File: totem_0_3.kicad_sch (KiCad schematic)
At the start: 88 parts, among them J1 MJ-4PP-9, J2 MJ-4PP-9, U1 xiao-ble, U2 xiao-ble

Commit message: Switch from matrix switches to direct connect
Added two rp2040's to schema
Leaving out lables on rp2040 to make routing easier later
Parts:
- removed DL1, DL10, DL11, DL12, DL13, DL14, DL15, DL16, DL17, DL18, DL19, DL2, DL3, DL4, DL5, DL6, DL7, DL8, DL9, DR1, DR10, DR11, DR12, DR13, DR14, DR15, DR16, DR17, DR18, DR19, DR2, DR3, DR4, DR5, DR6, DR7, DR8, DR9: D_Small, TOTEMlib:Diode_SOD123, symbol Device:D_Small
- added U3, U4: RP2040, Package_DFN_QFN:QFN-56-1EP_7x7mm_P0.4mm_EP3.2x3.2mm, symbol MCU_RaspberryPi:RP2040
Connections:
- net COL0_L: no longer SWL1.1, SWL11.1, SWL16.1, SWL6.1
- net COL0_R: no longer SWR1.1, SWR11.1, SWR16.1, SWR6.1
- net COL1_L: no longer SWL12.1, SWL2.1, SWL7.1
- net COL1_R: no longer SWR12.1, SWR2.1, SWR7.1
- net COL2_L: no longer SWL13.1, SWL17.1, SWL3.1, SWL8.1
- net COL2_R: no longer SWR13.1, SWR17.1, SWR3.1, SWR8.1
- net COL3_L: no longer SWL14.1, SWL18.1, SWL4.1, SWL9.1
- net COL3_R: no longer SWR14.1, SWR18.1, SWR4.1, SWR9.1
- net COL4_L: no longer SWL10.1, SWL15.1, SWL19.1, SWL5.1
- net COL4_R: no longer SWR10.1, SWR15.1, SWR19.1, SWR5.1
- net GND_L: now also SWL1.2, SWL10.2, SWL11.2, SWL13.2, SWL14.2, SWL15.2, SWL16.2, SWL17.2, SWL18.2, SWL19.2, SWL3.2, SWL4.2, SWL5.2, SWL6.2, SWL7.2, SWL8.2, SWL9.2
- net GND_R: now also SWR1.2, SWR10.2, SWR11.2, SWR12.2, SWR13.2, SWR14.2, SWR15.2, SWR16.2, SWR17.2, SWR18.2, SWR19.2, SWR2.2, SWR3.2, SWR4.2, SWR5.2, SWR6.2, SWR7.2, SWR8.2, SWR9.2
- new net: U3.1 (IOVDD), U3.10 (IOVDD), U3.22 (IOVDD), U3.33 (IOVDD), U3.42 (IOVDD), U3.49 (IOVDD)
- new net: U3.23 (DVDD), U3.50 (DVDD)
- new net: U4.1 (IOVDD), U4.10 (IOVDD), U4.22 (IOVDD), U4.33 (IOVDD), U4.42 (IOVDD), U4.49 (IOVDD)
- new net: U4.23 (DVDD), U4.50 (DVDD)
- new net SWL1: SWL1.1
- new net SWL10: SWL10.1
- new net SWL11: SWL11.1
- new net SWL12: SWL12.1
- new net SWL13: SWL13.1
- new net SWL14: SWL14.1
- new net SWL15: SWL15.1
- new net SWL16: SWL16.1, SWL6.1
- new net SWL17: SWL17.1
- new net SWL18: SWL18.1
- new net SWL19: SWL19.1
- new net SWL3: SWL3.1
- new net SWL4: SWL4.1
- new net SWL5: SWL5.1
- new net SWL7: SWL7.1
- new net SWL8: SWL8.1
- new net SWL9: SWL9.1
- new net SWR1: SWR1.1
- new net SWR10: SWR10.1
- new net SWR11: SWR11.1
- new net SWR12: SWR12.1
- new net SWR13: SWR13.1
- new net SWR14: SWR14.1
- new net SWR15: SWR15.1
- new net SWR16: SWR16.1
- new net SWR17: SWR17.1
- new net SWR18: SWR18.1
- new net SWR19: SWR19.1
- new net SWR2: SWR2.1
- new net SWR3: SWR3.1
- new net SWR4: SWR4.1
- new net SWR5: SWR5.1
- new net SWR6: SWR6.1
- new net SWR7: SWR7.1
- new net SWR8: SWR8.1
- new net SWR9: SWR9.1
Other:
- note added: "S W I T C H E S"
- note removed: "S W I T C H M A T R I X"
- moved on the sheet: BAT+1, BATGND1, PSW1, SWL1, SWL10, SWL11, SWL12, SWL13, SWL14, SWL15, SWL16, SWL17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

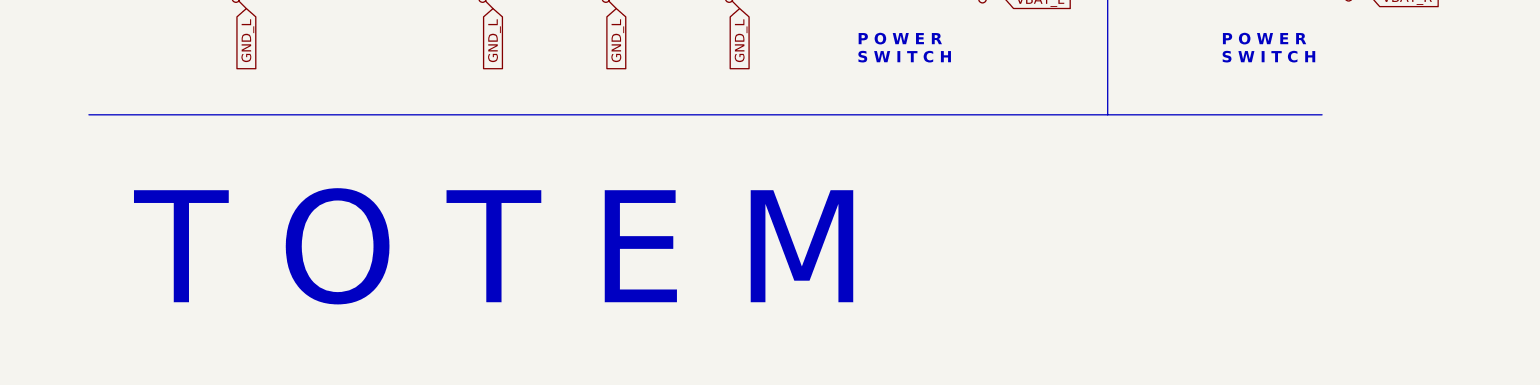
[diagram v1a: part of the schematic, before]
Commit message: Change schematic info
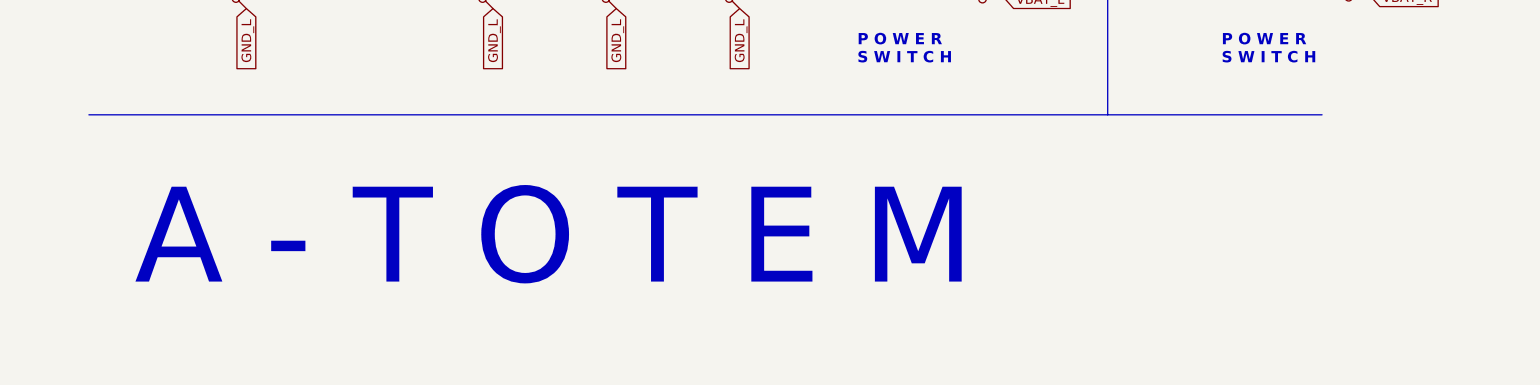
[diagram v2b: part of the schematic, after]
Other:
- note added: "A - T O T E M"
- note removed: "T O T E M"
- title: TOTEM split keyboard -> RP2040 TOTEM split keyboard
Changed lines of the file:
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@@
 	(paper "A4")
 	(title_block
-		(title "TOTEM split keyboard")
+		(title "RP2040 TOTEM split keyboard")
 		(date "2022-11-09")
 		(rev "0.3")
-		(comment 1 "made by GEIST")
+		(comment 1 "https://github.com/GEIGEIGEIST/TOTEM")
+		(comment 2 "original made by GEIST")
+		(comment 3 "made by A-Helberg")
 	)
 	(no_connect
@@
 		)
 	)
-	(text "T O T E M"
+	(text "A - T O T E M"
 		(exclude_from_sim no)
-		(at 18.034 195.072 0)
+		(at 18.034 192.024 0)
 		(effects
 			(font
-				(size 15 15)
+				(size 12.7 12.7)
 			)
 			(justify left bottom)
